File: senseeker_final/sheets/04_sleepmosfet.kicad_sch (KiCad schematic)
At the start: 8 parts, among them P3 1.27mm/1*3p, Q8 CJQ4435, U4 TPL5110DDCT

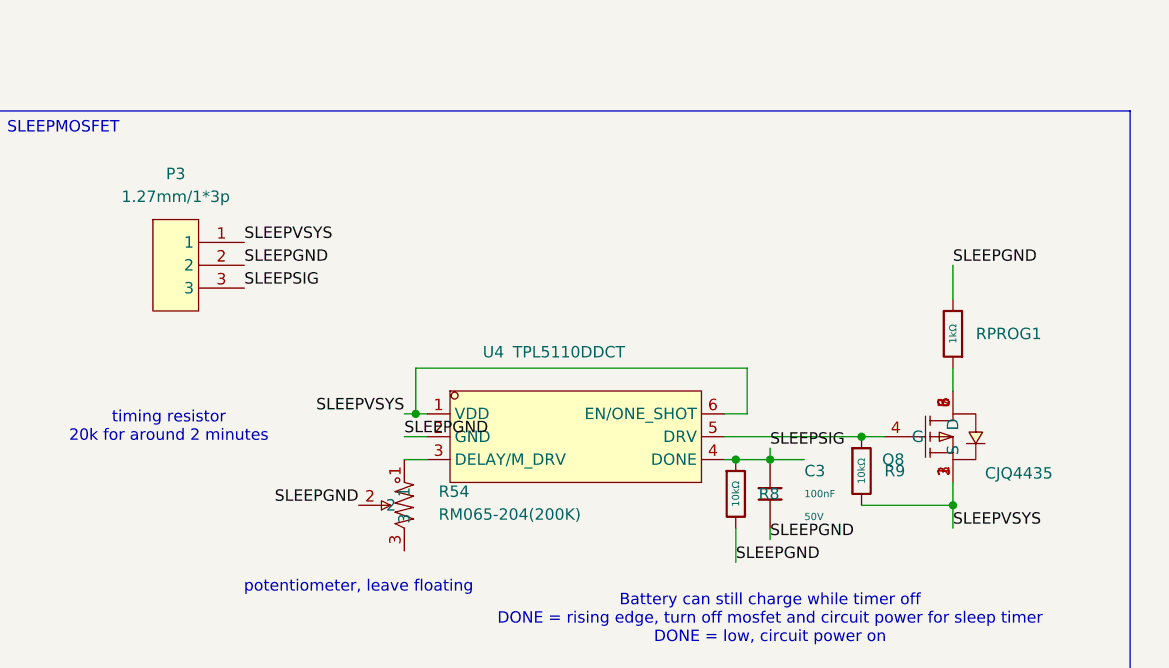
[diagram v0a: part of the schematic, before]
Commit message: formatting changes for LM2596, now ready to branch of off and make our seperate PCB and then compare
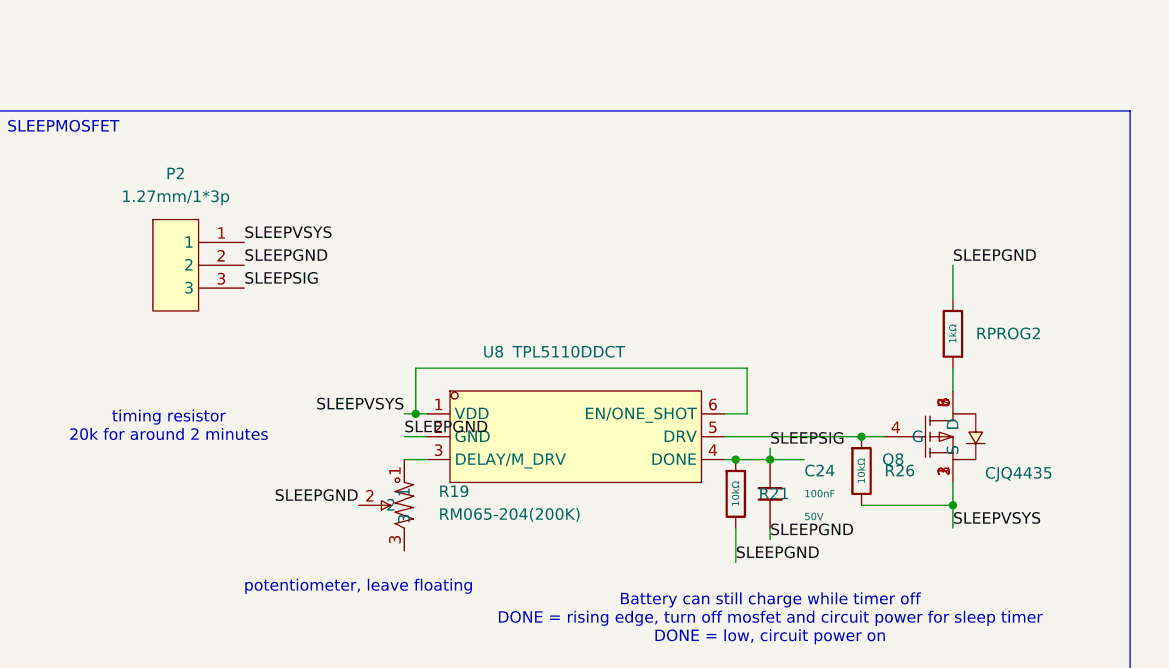
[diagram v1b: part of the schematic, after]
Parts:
- renumbered C3 to C24, P3 to P2, R54 to R19, R8 to R21, R9 to R26, RPROG1 to RPROG2, U4 to U8
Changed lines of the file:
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@@
 		(dnp no)
 		(fields_autoplaced yes)
-		(property "Reference" "R9"
+		(property "Reference" "R26"
 			(at 179.07 113.0299 0)
 			(effects
@@
 			(project "senseeker_final"
 				(path "/529bc8a5-ffae-43ac-972d-caccc3afab85/46234f0e-61f2-45bf-9df2-e52d6b9d2e9e"
-					(reference "R9")
+					(reference "R26")
 					(unit 1)
 				)
@@
 		(dnp no)
 		(fields_autoplaced yes)
-		(property "Reference" "P3"
+		(property "Reference" "P2"
 			(at 100.33 80.01 0)
 			(effects
@@
 			(project "senseeker_final"
 				(path "/529bc8a5-ffae-43ac-972d-caccc3afab85/46234f0e-61f2-45bf-9df2-e52d6b9d2e9e"
-					(reference "P3")
+					(reference "P2")
 					(unit 1)
 				)
@@
 		(on_board yes)
 		(dnp no)
-		(property "Reference" "U4"
+		(property "Reference" "U8"
 			(at 135.636 99.822 0)
 			(effects
@@
 			(project "senseeker_final"
 				(path "/529bc8a5-ffae-43ac-972d-caccc3afab85/46234f0e-61f2-45bf-9df2-e52d6b9d2e9e"
-					(reference "U4")
+					(reference "U8")
 					(unit 1)
 				)
@@
 		(dnp no)
 		(fields_autoplaced yes)
-		(property "Reference" "R8"
+		(property "Reference" "R21"
 			(at 165.1 115.5699 0)
 			(effects
@@
 			(project "senseeker_final"
 				(path "/529bc8a5-ffae-43ac-972d-caccc3afab85/46234f0e-61f2-45bf-9df2-e52d6b9d2e9e"
-					(reference "R8")
+					(reference "R21")
 					(unit 1)
 				)
@@
 		(dnp no)
 		(fields_autoplaced yes)
-		(property "Reference" "C3"
+		(property "Reference" "C24"
 			(at 170.18 113.0299 0)
 			(effects
@@
 			(project "senseeker_final"
 				(path "/529bc8a5-ffae-43ac-972d-caccc3afab85/46234f0e-61f2-45bf-9df2-e52d6b9d2e9e"
-					(reference "C3")
+					(reference "C24")
 					(unit 1)
 				)
@@
 		(dnp no)
 		(fields_autoplaced yes)
-		(property "Reference" "R54"
+		(property "Reference" "R19"
 			(at 129.54 115.3199 90)
 			(effects
@@
 			(project "senseeker_final"
 				(path "/529bc8a5-ffae-43ac-972d-caccc3afab85/46234f0e-61f2-45bf-9df2-e52d6b9d2e9e"
-					(reference "R54")
+					(reference "R19")
 					(unit 1)
 				)
@@
 		(dnp no)
 		(fields_autoplaced yes)
-		(property "Reference" "RPROG1"
+		(property "Reference" "RPROG2"
 			(at 189.23 97.7899 0)
 			(effects
@@
 			(project "senseeker_final"
 				(path "/529bc8a5-ffae-43ac-972d-caccc3afab85/46234f0e-61f2-45bf-9df2-e52d6b9d2e9e"
-					(reference "RPROG1")
-					(unit 1)
-				)
+					(reference "RPROG2")
+					(unit 1)
+				)
